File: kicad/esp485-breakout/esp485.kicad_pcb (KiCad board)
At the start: 2 copper layers, 25.4 x 25.4 mm, 22 parts, among them J1 Conn_01x08, J2 Conn_01x08, SW1 SW_Push, SW2 SW_Push, U1 MAX3485, U2 ESP-WROOM-02, U3 AMS1117-3.3

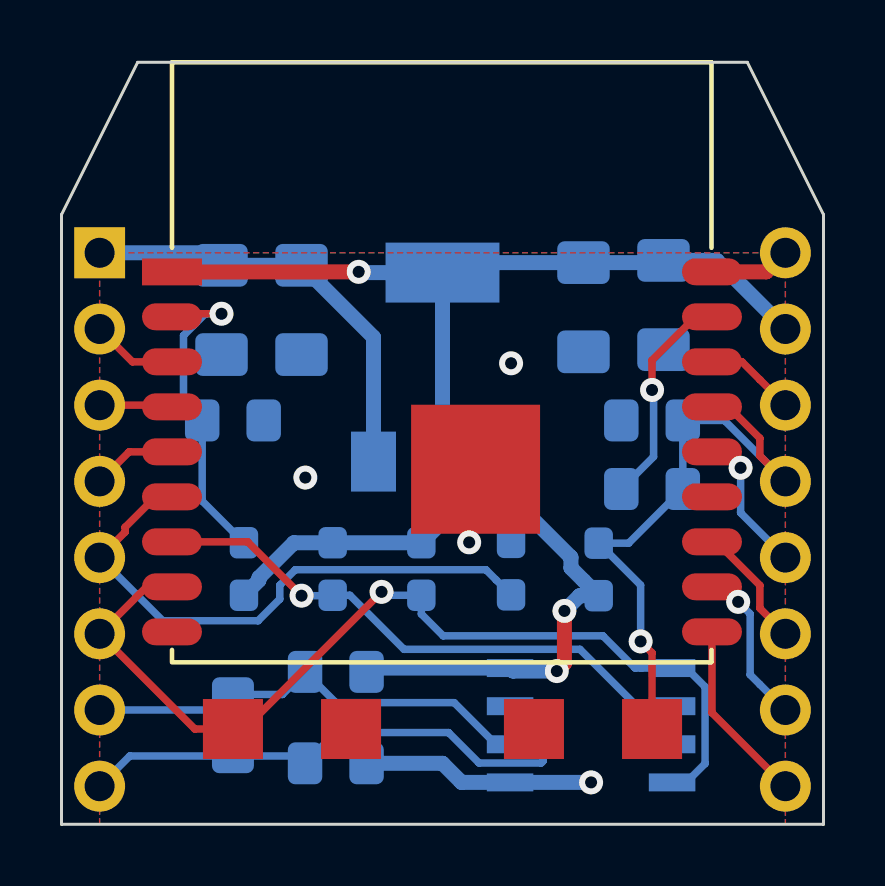
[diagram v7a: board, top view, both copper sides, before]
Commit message: make RS485/IO2 selectable
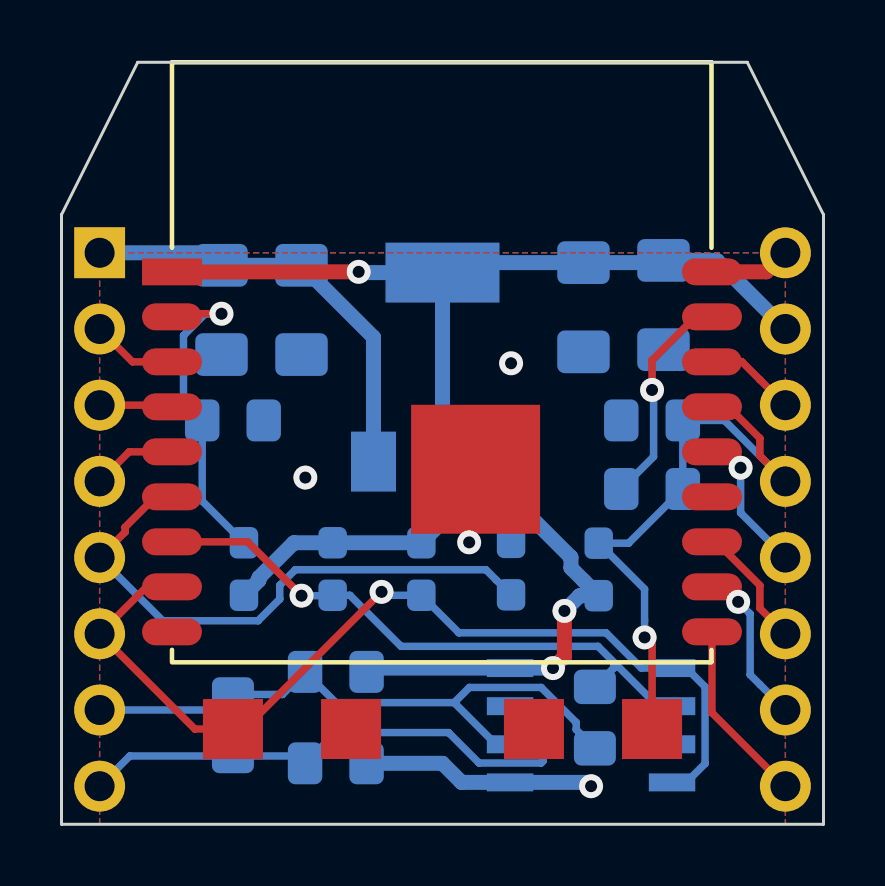
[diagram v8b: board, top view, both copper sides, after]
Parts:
- added R8: 0, Resistor_SMD:R_0805_2012Metric_Pad1.15x1.40mm_HandSolder, B.Cu at (146.1, 112.0)
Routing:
- net /A: track 15.2 -> 21.1 mm
- net /IO2: track 20.3 -> 21.4 mm
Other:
- board text added: "A/IO2"
- board text added: "VIN"
- board text removed: "A"
- board text removed: "VCC"
